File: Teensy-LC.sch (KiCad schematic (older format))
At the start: 29 parts, among them Q201 SSM3K329R, Q202 SSM3K329R, Q203 SSM3J334R, SW201 SW_Push, SW202 SW_Push, SW203 SW_Push, U201 LCD 2004A, U202 Teensy-LC

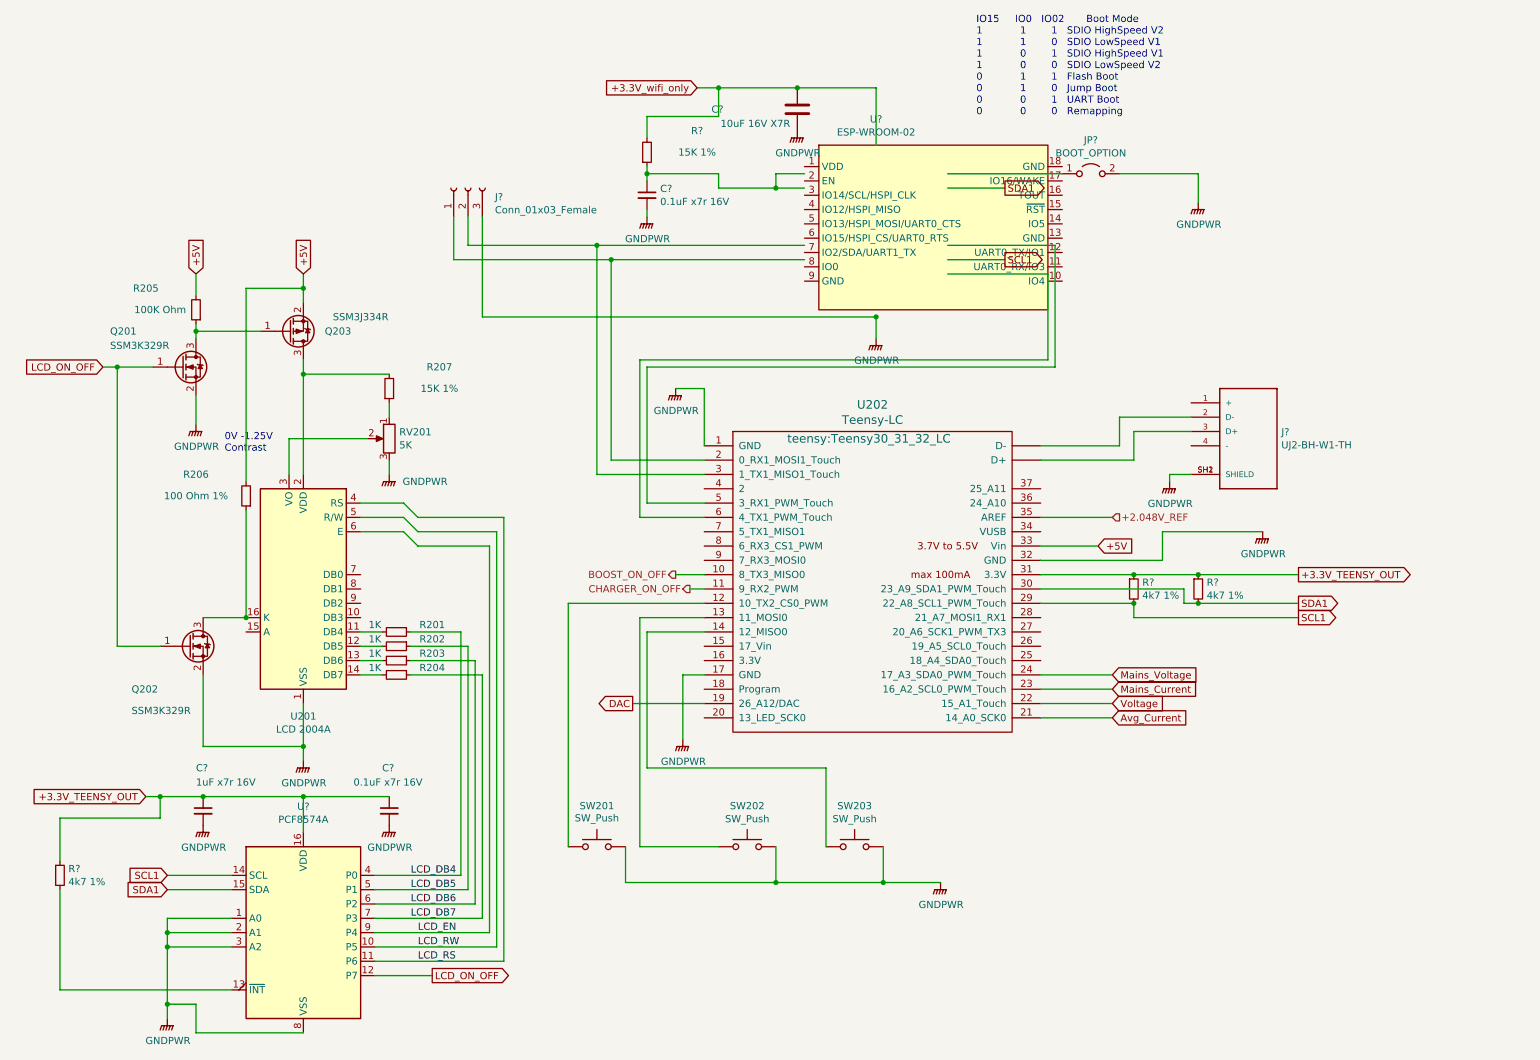
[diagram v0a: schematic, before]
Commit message: started routing backing up tonnes of changes,2.048V reference changed to 2.5V ref, to match ucc2800, cos to change to a version with a 2V feedback, would require me to update the Oscillator cap and resistor,and also recalulate the class 2 loop compensation components etc.  Move the location of the teensy LC and added the ESP-WROOM-o2 wifi module.
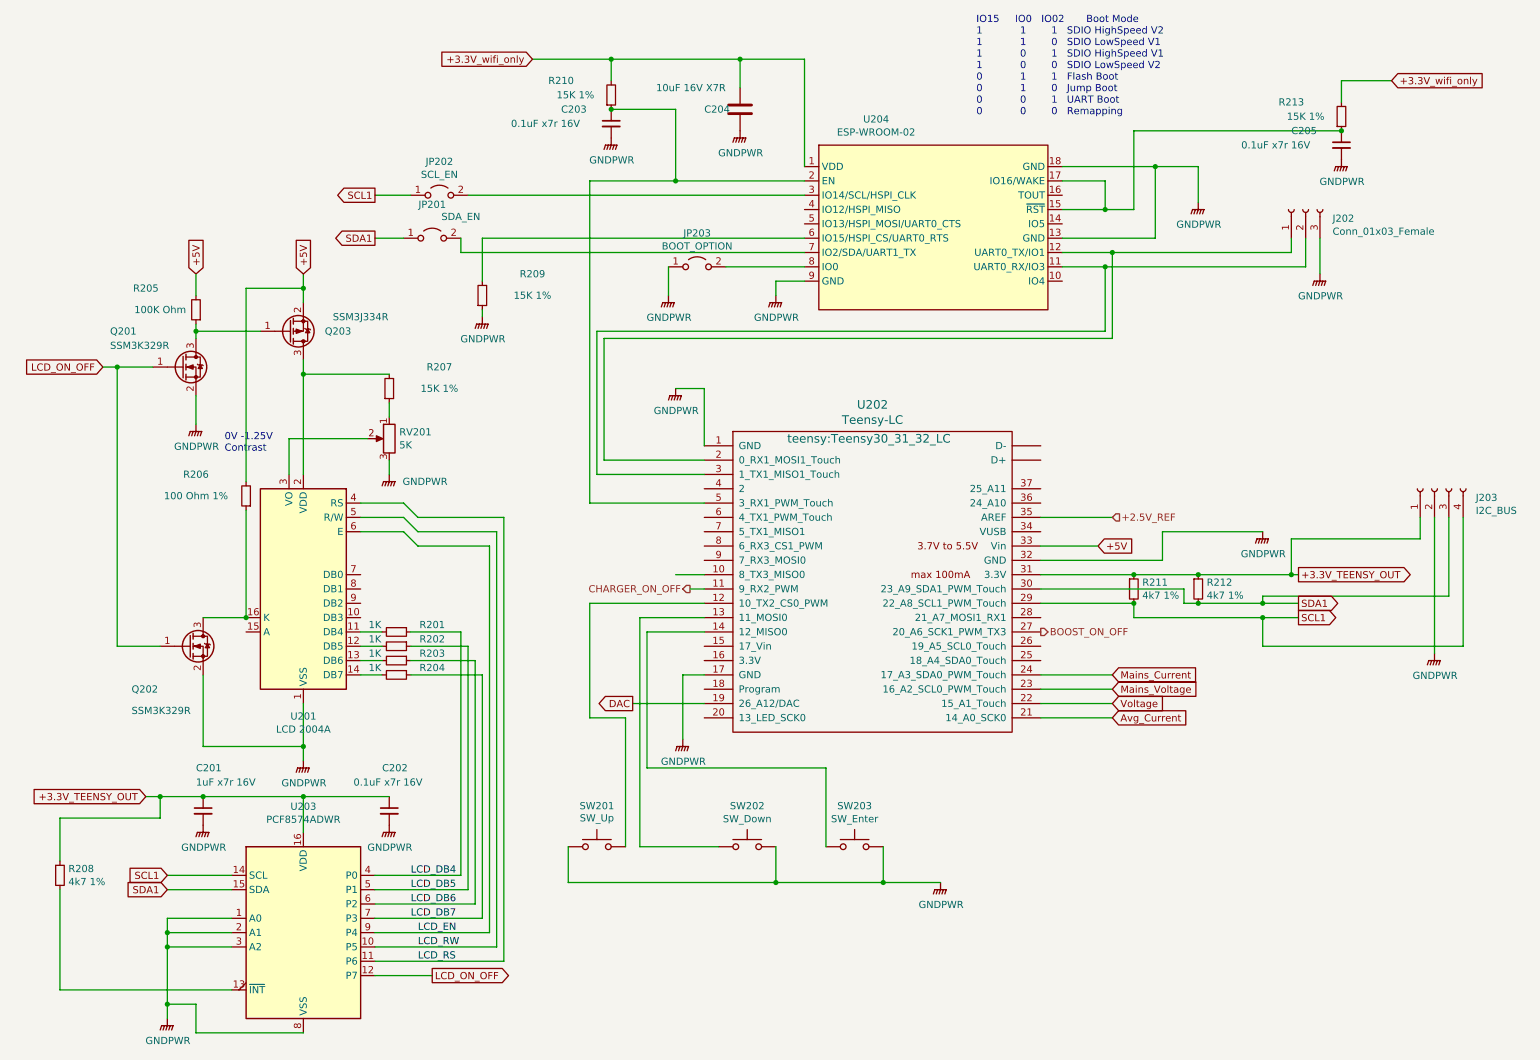
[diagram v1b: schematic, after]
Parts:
- removed J?: UJ2-BH-W1-TH, CUI_UJ2-BH-W1-TH, symbol UJ2-BH-W1-TH:UJ2-BH-W1-TH
- added C205: 0.1uF x7r 16V, Capacitors_SMD:C_0805_HandSoldering, symbol Device:C_Small
- added J203: I2C_BUS, Pin_Headers:Pin_Header_Straight_1x04_Pitch2.54mm, symbol Connector:Conn_01x04_Female
- added JP201: SDA_EN, Pin_Headers:Pin_Header_Straight_1x02_Pitch2.54mm, symbol Jumper:Jumper_2_Open
- added JP202: SCL_EN, Pin_Headers:Pin_Header_Straight_1x02_Pitch2.54mm, symbol Jumper:Jumper_2_Open
- added R209, R213: 15K 1%, Resistors_SMD:R_0805_HandSoldering, symbol Device:R_Small
- J202: renamed from J?; footprint (none) -> Pin_Headers:Pin_Header_Straight_1x03_Pitch2.54mm
- JP203: renamed from JP?; footprint Connect:PINHEAD1-2 -> Pin_Headers:Pin_Header_Straight_1x02_Pitch2.54mm
- SW201: value SW_Push -> SW_Up
- SW202: value SW_Push -> SW_Down
- SW203: value SW_Push -> SW_Enter
- U203: renamed from U?; value PCF8574A -> PCF8574ADWR; footprint (none) -> Housings_SOIC:SOIC-16W_7.5x10.3mm_Pitch1.27mm
- gave numbers to parts that had none: 9
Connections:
- net labels added: +2.5V_REF
- net labels removed: +2.048V_REF
- wire segments 170 -> 185
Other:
- moved on the sheet: C203, C204, J202, JP203, R210

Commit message: Almost finished the routing, an other backup commit git add *
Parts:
- U204: value ESP-WROOM-02 -> ESP-WROOM-02U; footprint RF_Module:ESP-WROOM-02 -> RF_Module_jl:MODULE_ESP-WROOM-02U
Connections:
- net LCD_EN: now also U201.6 (E)
- net LCD_RS: now also U201.4 (RS)
- net LCD_RW: now also U201.5 (R/W)
- net at U201.15 (A): now also R206.1
- net at Q202.3 (D), U201.16 (K): no longer R206.1
- net mcu_wifi_rx: now reaches J202.1 (Pin_1), U202.2 (0_RX1_MOSI1_Touch), U204.12 (UART0_TX/IO1)
- net mcu_wifi_tx: now reaches J202.2 (Pin_2), U202.3 (1_TX1_MISO1_Touch), U204.11 (UART0_RX/IO3)
- net wifi_en: now reaches C203.1, R210.1, U202.5 (3_RX1_PWM_Touch), U204.2 (EN)
- net ~reset: now reaches C205.1, R213.1, U204.15 (~RST), U204.17 (IO16/WAKE)
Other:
- moved on the sheet: Q202, R206
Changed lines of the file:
@@
 Text GLabel 8050 5250 2    50   Input ~ 0
 Mains_Voltage
-$Comp
-L Display_Character:NHD-0420H1Z U201
-U 1 1 5E86612A
-P 2400 4550
-F 0 "U201" H 2400 3661 50  0000 C CNN
-F 1 "LCD 2004A" H 2400 3570 50  0000 C CNN
-F 2 "Connect_jl:LCD2004_Pin_Header_Angled_1x16_Pitch2.54mm" H 2400 3650 50  0001 C CNN
-F 3 "/media/jlynch/SW_Preload/Users/jlynch/Downloads/DataSheets/LCD/2004A-RK-10290_410.pdf" H 2500 4450 50  0001 C CNN
-F 4 "http://www.adam-tech.com/downloader.php?p=PH1RB-XX-UA.pdf" H 2400 4550 50  0001 C CNN "Connector"
-	1    2400 4550
-	-1   0    0    -1
-$EndComp
 Text GLabel 2400 2350 1    50   Input ~ 0
 +5V
@@
 L Device:Q_NMOS_GSD Q?
 U 1 1 5F7AABC6
-P 1600 4950
+P 1600 5050
 AR Path="/5F7AABC6" Ref="Q?"  Part="1"
 AR Path="/5EF73D52/5F7AABC6" Ref="Q202"  Part="1"
-F 0 "Q202" H 1200 4650 50  0000 L CNN
-F 1 "SSM3K329R" H 1200 4500 50  0000 L CNN
-F 2 "Package_TO_SOT_SMD:SOT-23_Handsoldering" H 1800 5050 50  0001 C CNN
-F 3 "https://toshiba.semicon-storage.com/info/docget.jsp?did=2157&prodName=SSM3K329R" H 1600 4950 50  0001 C CNN
-	1    1600 4950
-	1    0    0    -1
-$EndComp
-Wire Wire Line
-	1700 5150 1700 5650
+F 0 "Q202" H 1200 4750 50  0000 L CNN
+F 1 "SSM3K329R" H 1200 4600 50  0000 L CNN
+F 2 "Package_TO_SOT_SMD:SOT-23_Handsoldering" H 1800 5150 50  0001 C CNN
+F 3 "https://toshiba.semicon-storage.com/info/docget.jsp?did=2157&prodName=SSM3K329R" H 1600 5050 50  0001 C CNN
+	1    1600 5050
+	1    0    0    -1
+$EndComp
+Wire Wire Line
+	1700 5250 1700 5650
 Wire Wire Line
 	1700 5650 2400 5650
@@
 Wire Wire Line
 	2400 5650 2400 5750
-Wire Wire Line
-	2000 4750 1700 4750
-Wire Wire Line
-	1000 3000 1100 3000
-Wire Wire Line
-	1400 4950 1100 4950
-Wire Wire Line
-	1100 4950 1100 3000
-Connection ~ 1100 3000
-Wire Wire Line
-	1100 3000 1350 3000
 $Comp
 L Device:R_Small R206
 U 1 1 5F7FE774
-P 2000 3900
-F 0 "R206" H 2350 3750 50  0000 C CNN
-F 1 "100 Ohm 1%" H 2350 3900 50  0000 C CNN
-F 2 "Resistors_SMD:R_0805_HandSoldering" H 2000 3900 50  0001 C CNN
-F 3 "~" H 2000 3900 50  0001 C CNN
-	1    2000 3900
+P 1850 3900
+F 0 "R206" H 2200 3750 50  0000 C CNN
+F 1 "100 Ohm 1%" H 2200 3900 50  0000 C CNN
+F 2 "Resistors_SMD:R_0805_HandSoldering" H 1850 3900 50  0001 C CNN
+F 3 "~" H 1850 3900 50  0001 C CNN
+	1    1850 3900
 	-1   0    0    1
 $EndComp
-Wire Wire Line
-	2400 2350 2400 2450
-Wire Wire Line
-	2000 3800 2000 2450
-Wire Wire Line
-	2000 2450 2400 2450
-Connection ~ 2400 2450
-Wire Wire Line
-	2400 2450 2400 2550
-Wire Wire Line
-	2000 4000 2000 4750
 $Comp
 L Device:R_POT RV201
@@
 Wire Wire Line
 	7550 5350 8050 5350
-Entry Wire Line
-	3200 4050 3100 3950
-Entry Wire Line
-	3100 4150 3200 4250
-Entry Wire Line
-	3100 4050 3200 4150
-Wire Wire Line
-	2800 3950 3100 3950
-Wire Wire Line
-	2800 4050 3100 4050
-Wire Wire Line
-	2800 4150 3100 4150
 Text Label 3200 7150 0    50   ~ 0
 LCD_RS
@@
 P 6400 2050
 F 0 "U204" H 6400 2831 50  0000 C CNN
-F 1 "ESP-WROOM-02" H 6400 2740 50  0000 C CNN
-F 2 "RF_Module:ESP-WROOM-02" H 7000 1500 50  0001 C CNN
+F 1 "ESP-WROOM-02U" H 6400 2740 50  0000 C CNN
+F 2 "RF_Module_jl:MODULE_ESP-WROOM-02U" H 7000 1500 50  0001 C CNN
 F 3 "https://www.espressif.com/sites/default/files/documentation/0c-esp-wroom-02_datasheet_en.pdf" H 6450 3550 50  0001 C CNN
 	1    6400 2050
@@
 Wire Wire Line
 	5300 6350 4750 6350
-Connection ~ 2000 4750
 Wire Wire Line
 	2900 6550 3500 6550
@@
 	2900 6950 3700 6950
 Wire Wire Line
-	3700 6950 3700 4250
-Wire Wire Line
-	3700 4250 3200 4250
-Wire Wire Line
 	2900 7050 3750 7050
-Wire Wire Line
-	3750 7050 3750 4150
-Wire Wire Line
-	3750 4150 3200 4150
-Wire Wire Line
-	3800 7150 3800 4050
-Wire Wire Line
-	3800 4050 3200 4050
 Text Label 3150 6550 0    50   ~ 0
 LCD_DB4
@@
 Wire Wire Line
 	4400 4650 5200 4650
+Text Label 4600 3950 0    50   ~ 0
+wifi_en
+Text Label 8450 1350 0    50   ~ 0
+~reset
+Text Label 4600 3750 0    50   ~ 0
+mcu_wifi_tx
+Text Label 4600 3650 0    50   ~ 0
+mcu_wifi_rx
+Text Label 7750 1700 0    50   ~ 0
+~wake_out
+$Comp
+L Display_Character:NHD-0420H1Z U201
+U 1 1 5E86612A
+P 2400 4550
+F 0 "U201" H 2400 3661 50  0000 C CNN
+F 1 "LCD 2004A" H 2400 3570 50  0000 C CNN
+F 2 "Connect_jl:LCD2004_Pin_Header_Angled_1x16_Pitch2.54mm" H 2400 3650 50  0001 C CNN
+F 3 "/media/jlynch/SW_Preload/Users/jlynch/Downloads/DataSheets/LCD/2004A-RK-10290_410.pdf" H 2500 4450 50  0001 C CNN
+F 4 "http://www.adam-tech.com/downloader.php?p=PH1RB-XX-UA.pdf" H 2400 4550 50  0001 C CNN "Connector"
+	1    2400 4550
+	-1   0    0    -1
+$EndComp
+Wire Wire Line
+	2400 2350 2400 2500
+Wire Wire Line
+	2400 2500 1850 2500
+Wire Wire Line
+	1850 2500 1850 3800
+Connection ~ 2400 2500
+Wire Wire Line
+	2400 2500 2400 2550
+Wire Wire Line
+	1850 4000 1850 4850
+Wire Wire Line
+	1850 4850 2000 4850
+Wire Wire Line
+	2000 4750 1700 4750
+Wire Wire Line
+	1700 4750 1700 4850
+Wire Wire Line
+	1000 3000 1150 3000
+Wire Wire Line
+	1150 3000 1150 5050
+Wire Wire Line
+	1150 5050 1400 5050
+Connection ~ 1150 3000
+Wire Wire Line
+	1150 3000 1350 3000
+Wire Wire Line
+	3800 3950 2800 3950
+Wire Wire Line
+	3800 3950 3800 7150
+Wire Wire Line
+	2800 4050 3750 4050
+Wire Wire Line
+	3750 4050 3750 7050
+Wire Wire Line
+	2800 4150 3700 4150
+Wire Wire Line
+	3700 4150 3700 6950
 $EndSCHEMATC

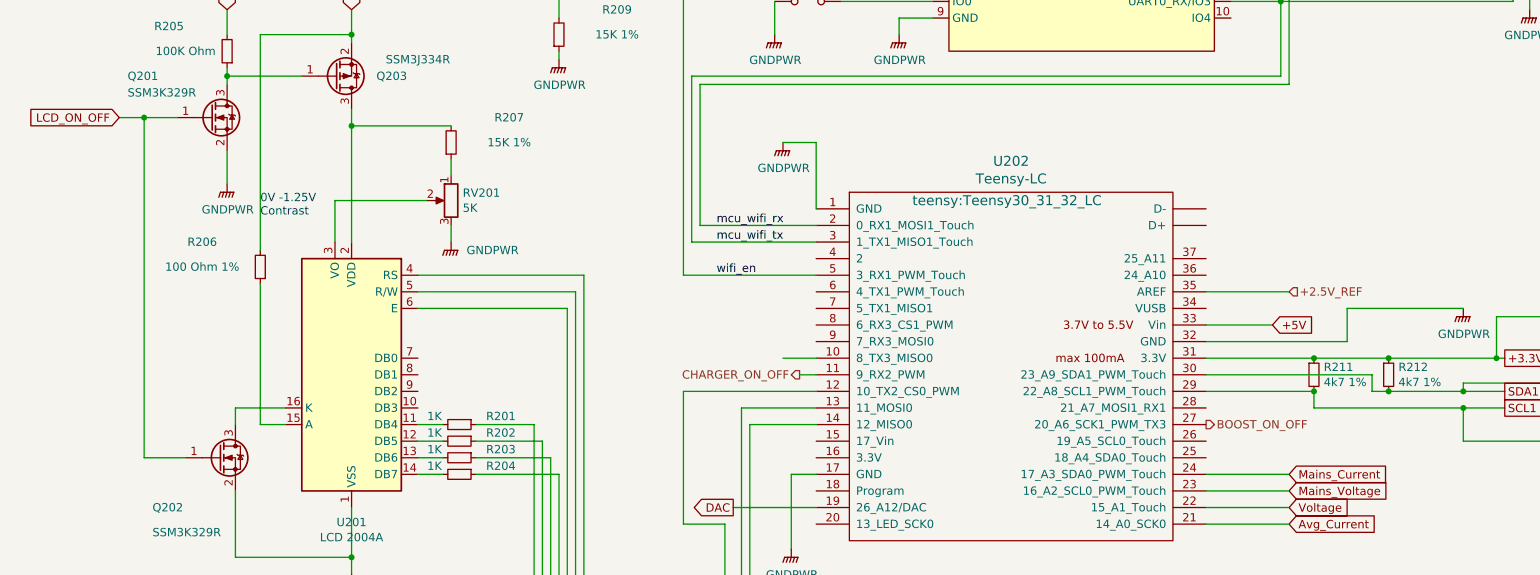
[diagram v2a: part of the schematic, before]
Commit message: added testpoints
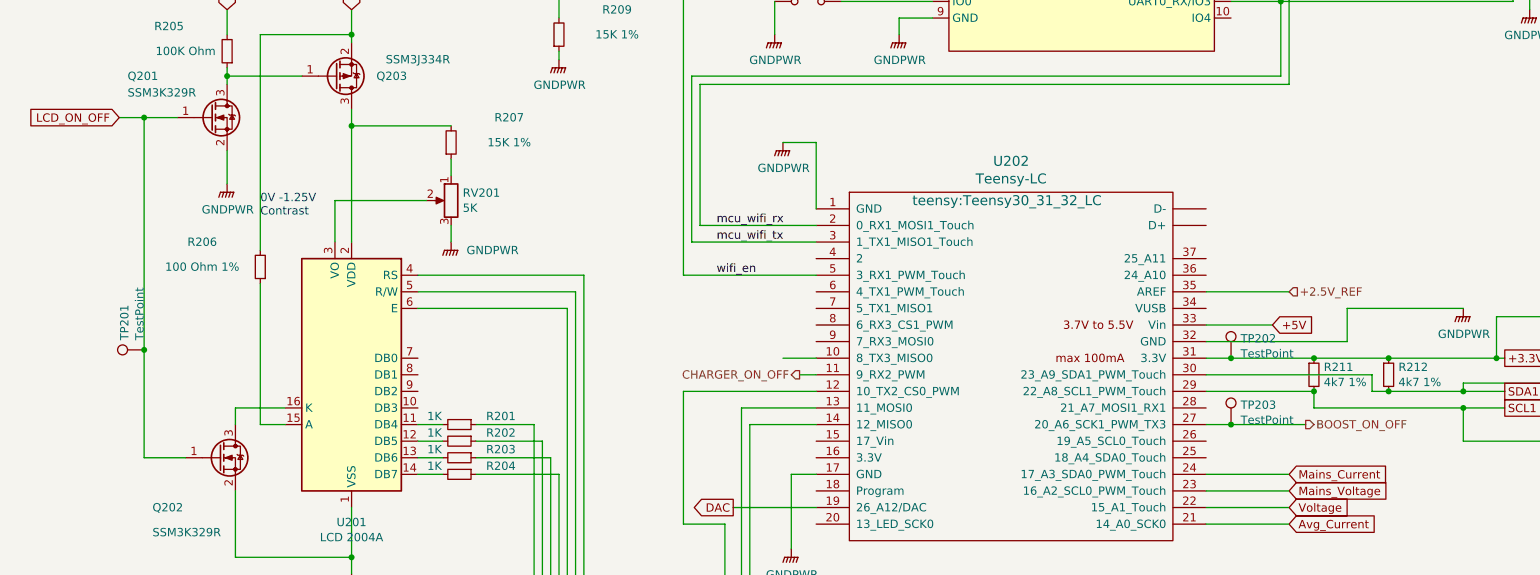
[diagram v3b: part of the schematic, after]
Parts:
- added TP201, TP202, TP203: TestPoint, Measurement_Points:Measurement_Point_Square-SMD-Pad_Big, symbol Connector:TestPoint
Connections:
- net +3.3V_TEENSY_OUT: now also TP202.1
- net BOOST_ON_OFF: now also TP203.1
- net LCD_ON_OFF: now also TP201.1
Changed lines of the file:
@@
 Text HLabel 5100 4550 0    50   Output ~ 0
 CHARGER_ON_OFF
-Text HLabel 7550 4850 2    50   Output ~ 0
+Text HLabel 8150 4850 2    50   Output ~ 0
 BOOST_ON_OFF
 $Comp
@@
 	8200 4450 8650 4450
 Wire Wire Line
-	7550 4450 8200 4450
+	7550 4450 7700 4450
 Wire Wire Line
 	7550 4350 8400 4350
@@
 	1000 3000 1150 3000
 Wire Wire Line
-	1150 3000 1150 5050
+	1150 3000 1150 4400
 Wire Wire Line
 	1150 5050 1400 5050
@@
 Wire Wire Line
 	3700 4150 3700 6950
+$Comp
+L Connector:TestPoint TP?
+U 1 1 604D2532
+P 1150 4400
+AR Path="/5EBD6442/604D2532" Ref="TP?"  Part="1"
+AR Path="/5EF73D52/604D2532" Ref="TP201"  Part="1"
+F 0 "TP201" H 1208 4518 50  0000 L CNN
+F 1 "TestPoint" H 1208 4427 50  0000 L CNN
+F 2 "Measurement_Points:Measurement_Point_Square-SMD-Pad_Big" H 1350 4400 50  0001 C CNN
+F 3 "~" H 1350 4400 50  0001 C CNN
+	1    1150 4400
+	0    -1   -1   0
+$EndComp
+$Comp
+L Connector:TestPoint TP?
+U 1 1 604DC721
+P 7700 4450
+AR Path="/5EBD6442/604DC721" Ref="TP?"  Part="1"
+AR Path="/5EF73D52/604DC721" Ref="TP202"  Part="1"
+F 0 "TP202" H 7758 4568 50  0000 L CNN
+F 1 "TestPoint" H 7758 4477 50  0000 L CNN
+F 2 "Measurement_Points:Measurement_Point_Square-SMD-Pad_Big" H 7900 4450 50  0001 C CNN
+F 3 "~" H 7900 4450 50  0001 C CNN
+	1    7700 4450
+	1    0    0    -1
+$EndComp
+Connection ~ 7700 4450
+Wire Wire Line
+	7700 4450 8200 4450
+Wire Wire Line
+	7550 4850 7700 4850
+$Comp
+L Connector:TestPoint TP?
+U 1 1 604F5CFE
+P 7700 4850
+AR Path="/5EBD6442/604F5CFE" Ref="TP?"  Part="1"
+AR Path="/5EF73D52/604F5CFE" Ref="TP203"  Part="1"
+F 0 "TP203" H 7758 4968 50  0000 L CNN
+F 1 "TestPoint" H 7758 4877 50  0000 L CNN
+F 2 "Measurement_Points:Measurement_Point_Square-SMD-Pad_Big" H 7900 4850 50  0001 C CNN
+F 3 "~" H 7900 4850 50  0001 C CNN
+	1    7700 4850
+	1    0    0    -1
+$EndComp
+Connection ~ 7700 4850
+Wire Wire Line
+	7700 4850 8150 4850
+Connection ~ 1150 4400
+Wire Wire Line
+	1150 4400 1150 5050
 $EndSCHEMATC
